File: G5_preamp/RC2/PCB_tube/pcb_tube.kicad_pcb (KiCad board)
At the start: 2 copper layers, 100 x 47 mm, 31 parts, among them J1 PSU_TUBE, J2 PCB_TUBE, J3 OT

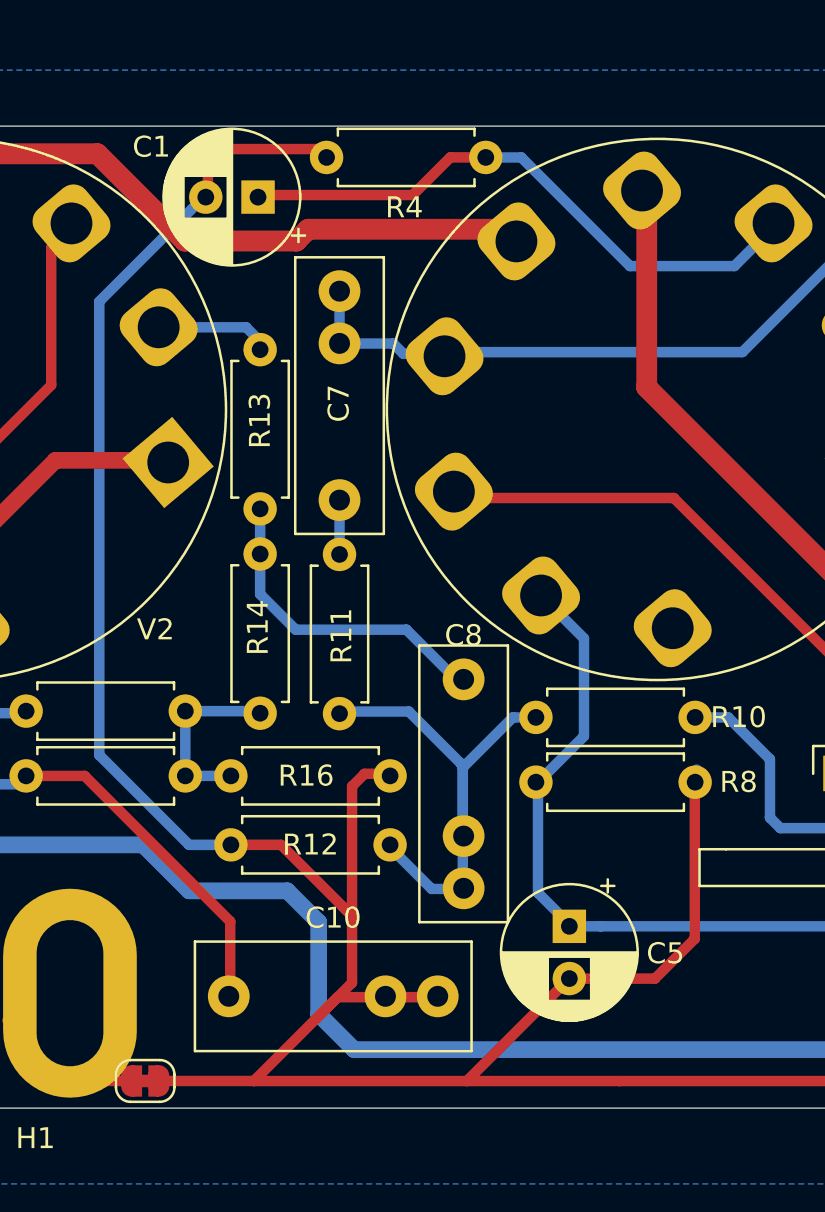
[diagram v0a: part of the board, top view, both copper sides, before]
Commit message: DC jack Polarity change
DC Jack polarity change and some capacitor footprint mod
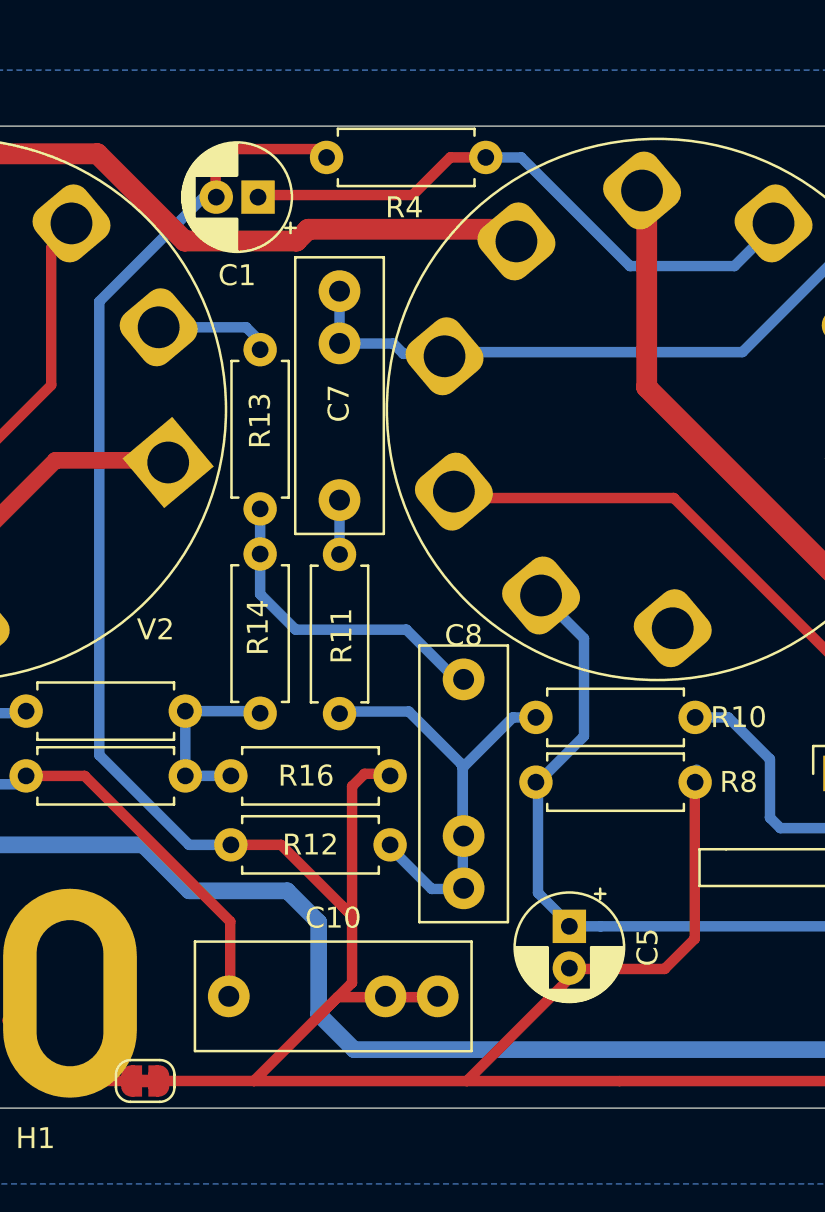
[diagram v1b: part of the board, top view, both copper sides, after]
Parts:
- C1: footprint Capacitor_THT:CP_Radial_D6.3mm_P2.50mm -> Capacitor_THT:CP_Radial_D5.0mm_P2.00mm
- C18: value 22µF/350v -> 22µF/400v
- C19: value 10µF/350v -> 10µF/400v
- C5: value 1µF/25v -> 1µF/50v; footprint Capacitor_THT:CP_Radial_D6.3mm_P2.50mm -> Capacitor_THT:CP_Radial_D5.0mm_P2.00mm
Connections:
- C7 pad 3: Net-(C7-Pad2) -> (no net)
